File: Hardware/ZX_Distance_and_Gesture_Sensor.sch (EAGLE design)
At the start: 48 parts, among them Q1 MMBT2222A, Q2 MOSFET-NCHANNEL2N7002PW, U1 BRM-2508VERT

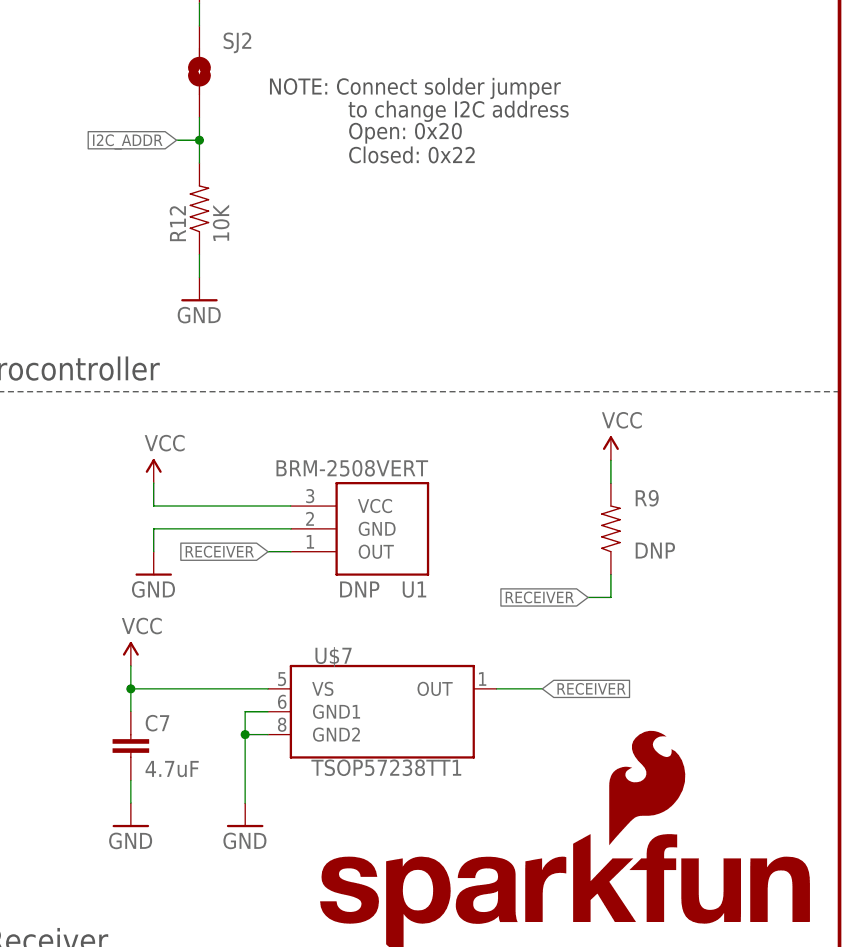
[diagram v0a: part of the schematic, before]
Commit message: Changed SMT receiver to DNP and removed DNP from PTH receiver and pullup resistor.
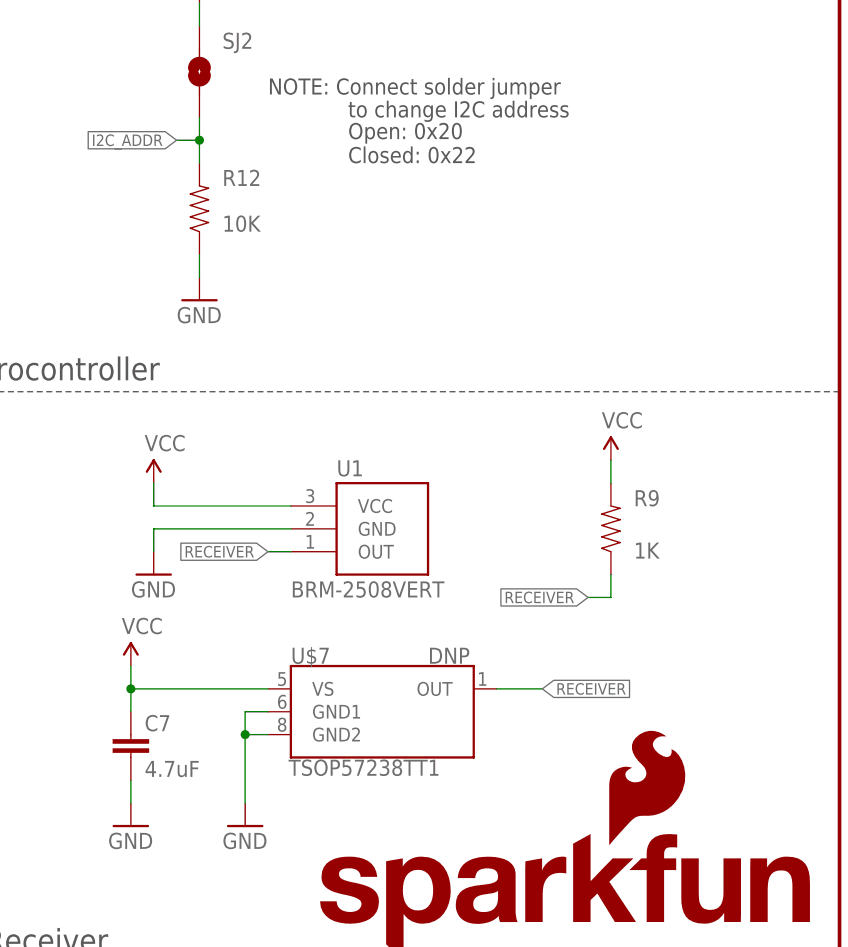
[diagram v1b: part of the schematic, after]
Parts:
- R9: value DNP -> 1K; device SparkFun-Resistors:RESISTOR0603 -> SparkFun-Resistors:1KOHM1/10W1%(0603)
- U$7: PLACE (none) -> DNP
- U1: PLACE DNP -> (none)
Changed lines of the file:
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@@
 <setting verticaltext="up"/>
 </settings>
-<grid distance="0.1" unitdist="inch" unit="inch" style="lines" multiple="1" display="no" altdistance="0.01" altunitdist="inch" altunit="inch"/>
+<grid distance="0.1" unitdist="inch" unit="inch" style="lines" multiple="1" display="yes" altdistance="0.01" altunitdist="inch" altunit="inch"/>
 <layers>
 <layer number="1" name="Top" color="4" fill="1" visible="no" active="no"/>
@@
 <part name="U$3" library="SparkFun-DiscreteSemi" deviceset="DMC2700UDM" device=""/>
 <part name="U$4" library="SparkFun-DiscreteSemi" deviceset="DMC2700UDM" device=""/>
-<part name="U$7" library="SparkFun-Sensors" deviceset="TSOP57238TT1" device=""/>
+<part name="U$7" library="SparkFun-Sensors" deviceset="TSOP57238TT1" device="">
+<attribute name="PLACE" value="DNP"/>
+</part>
 <part name="JP1" library="SparkFun-Connectors" deviceset="M06" device="NO_SILK"/>
 <part name="JP3" library="SparkFun-Connectors" deviceset="M03" device="1X03_NO_SILK"/>
@@
 <part name="SUPPLY10" library="SparkFun-Aesthetics" deviceset="VCC" device=""/>
 <part name="GND10" library="SparkFun-Aesthetics" deviceset="GND" device=""/>
-<part name="R9" library="SparkFun-Resistors" deviceset="RESISTOR" device="0603" value="DNP"/>
+<part name="R9" library="SparkFun-Resistors" deviceset="1KOHM1/10W1%(0603)" device="" value="1K"/>
 <part name="C7" library="SparkFun-Capacitors" deviceset="4.7UF-6.3V-10%(0603)" device="0603" value="4.7uF"/>
 <part name="GND11" library="SparkFun-Aesthetics" deviceset="GND" device=""/>
@@
 <part name="TP4" library="SparkFun-Passives" deviceset="TEST-POINT" device="3X4" value="TEST-POINT3X4"/>
 <part name="TP5" library="SparkFun-Passives" deviceset="TEST-POINT" device="3X4" value="TEST-POINT3X4"/>
-<part name="U1" library="SparkFun-Sensors" deviceset="BRM-2508" device="VERT">
-<attribute name="PLACE" value="DNP"/>
-</part>
+<part name="U1" library="SparkFun-Sensors" deviceset="BRM-2508" device="VERT"/>
 <part name="SUPPLY16" library="SparkFun-Aesthetics" deviceset="VCC" device=""/>
 <part name="GND16" library="SparkFun-Aesthetics" deviceset="GND" device=""/>
@@
 <instance part="U$3" gate="G$1" x="22.86" y="111.76"/>
 <instance part="U$4" gate="G$1" x="88.9" y="111.76"/>
-<instance part="U$7" gate="G$1" x="198.12" y="63.5"/>
+<instance part="U$7" gate="G$1" x="198.12" y="63.5" smashed="yes">
+<attribute name="NAME" x="187.96" y="68.834" size="1.778" layer="95"/>
+<attribute name="VALUE" x="187.706" y="56.388" size="1.778" layer="96"/>
+<attribute name="PLACE" x="203.2" y="68.834" size="1.778" layer="96"/>
+</instance>
 <instance part="JP1" gate="G$1" x="12.7" y="154.94" smashed="yes">
 <attribute name="VALUE" x="7.62" y="144.78" size="1.778" layer="96"/>
@@
 </instance>
 <instance part="SUPPLY13" gate="G$1" x="73.66" y="177.8"/>
-<instance part="R12" gate="G$1" x="177.8" y="119.38" rot="R90"/>
+<instance part="R12" gate="G$1" x="177.8" y="119.38" smashed="yes" rot="R90">
+<attribute name="NAME" x="180.34" y="121.92" size="1.778" layer="95"/>
+<attribute name="VALUE" x="180.34" y="116.84" size="1.778" layer="96"/>
+</instance>
 <instance part="GND15" gate="1" x="177.8" y="109.22"/>
 <instance part="SJ2" gate="1" x="177.8" y="134.62" smashed="yes" rot="R90">
@@
 </instance>
 <instance part="U1" gate="G$1" x="198.12" y="83.82" smashed="yes" rot="R180">
-<attribute name="PLACE" x="197.866" y="77.978" size="1.778" layer="96" rot="R180"/>
-<attribute name="NAME" x="203.2" y="77.978" size="1.778" layer="95" rot="R180"/>
-<attribute name="VALUE" x="203.2" y="91.44" size="1.778" layer="96" rot="R180"/>
+<attribute name="NAME" x="193.04" y="89.662" size="1.778" layer="95"/>
+<attribute name="VALUE" x="187.96" y="76.2" size="1.778" layer="96"/>
 </instance>
 <instance part="SUPPLY16" gate="G$1" x="172.72" y="88.9"/>

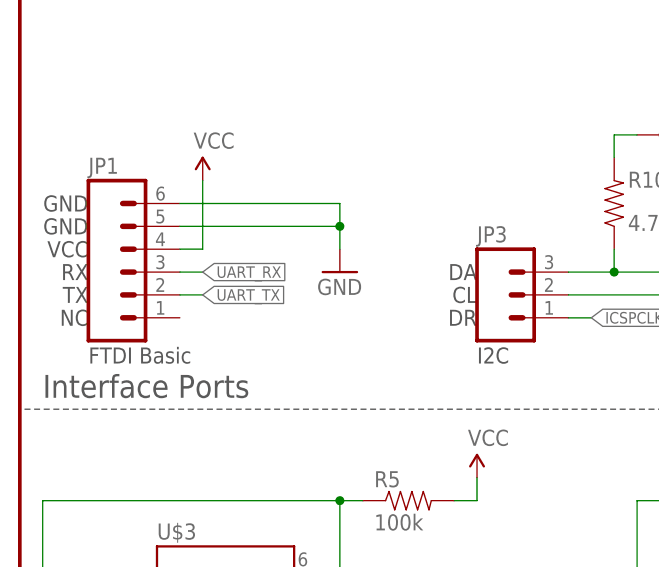
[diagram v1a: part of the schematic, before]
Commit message: Swapped TX/RX. Added diagonal trace from GND header to pour.
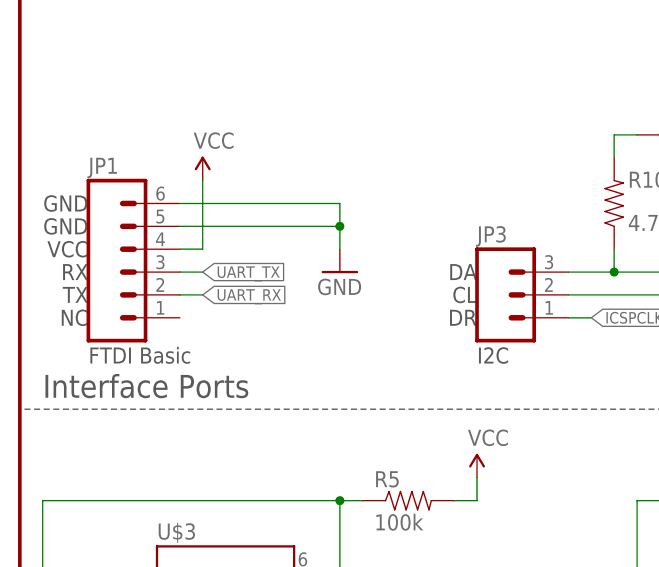
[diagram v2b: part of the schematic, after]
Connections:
- net UART_RX: now also JP1.2; no longer JP1.3
- net UART_TX: now also JP1.3; no longer JP1.2
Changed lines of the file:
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@@
 <net name="UART_TX" class="0">
+<segment>
+<pinref part="U$1" gate="G$1" pin="RC5"/>
+<wire x1="220.98" y1="157.48" x2="223.52" y2="157.48" width="0.1524" layer="91"/>
+<label x="223.52" y="157.48" size="1.27" layer="95" xref="yes"/>
+</segment>
+<segment>
+<pinref part="JP1" gate="G$1" pin="3"/>
+<wire x1="17.78" y1="154.94" x2="20.32" y2="154.94" width="0.1524" layer="91"/>
+<label x="20.32" y="154.94" size="1.27" layer="95" xref="yes"/>
+</segment>
+</net>
+<net name="UART_RX" class="0">
+<segment>
+<pinref part="U$1" gate="G$1" pin="RC4"/>
+<wire x1="220.98" y1="160.02" x2="223.52" y2="160.02" width="0.1524" layer="91"/>
+<label x="223.52" y="160.02" size="1.27" layer="95" xref="yes"/>
+</segment>
 <segment>
 <pinref part="JP1" gate="G$1" pin="2"/>
@@
 <label x="20.32" y="152.4" size="1.27" layer="95" xref="yes"/>
 </segment>
-<segment>
-<pinref part="U$1" gate="G$1" pin="RC5"/>
-<wire x1="220.98" y1="157.48" x2="223.52" y2="157.48" width="0.1524" layer="91"/>
-<label x="223.52" y="157.48" size="1.27" layer="95" xref="yes"/>
-</segment>
 </net>
-<net name="UART_RX" class="0">
-<segment>
-<pinref part="JP1" gate="G$1" pin="3"/>
-<wire x1="17.78" y1="154.94" x2="20.32" y2="154.94" width="0.1524" layer="91"/>
-<label x="20.32" y="154.94" size="1.27" layer="95" xref="yes"/>
-</segment>
-<segment>
-<pinref part="U$1" gate="G$1" pin="RC4"/>
-<wire x1="220.98" y1="160.02" x2="223.52" y2="160.02" width="0.1524" layer="91"/>
-<label x="223.52" y="160.02" size="1.27" layer="95" xref="yes"/>
-</segment>
-</net>

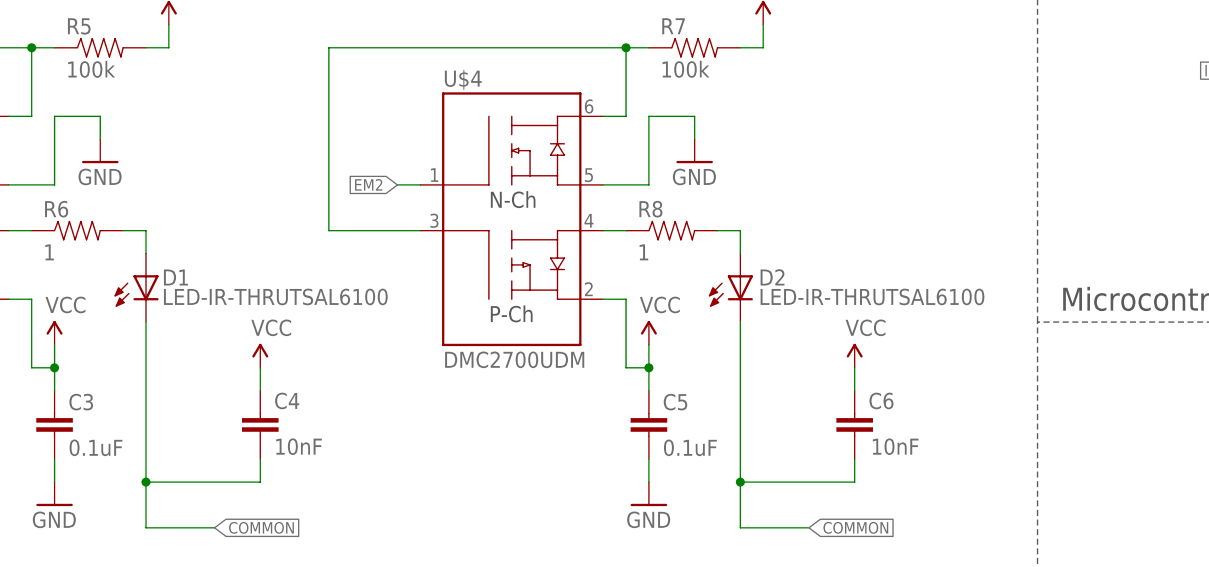
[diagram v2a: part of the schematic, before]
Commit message: Removed variant names on IR LEDs in schematic
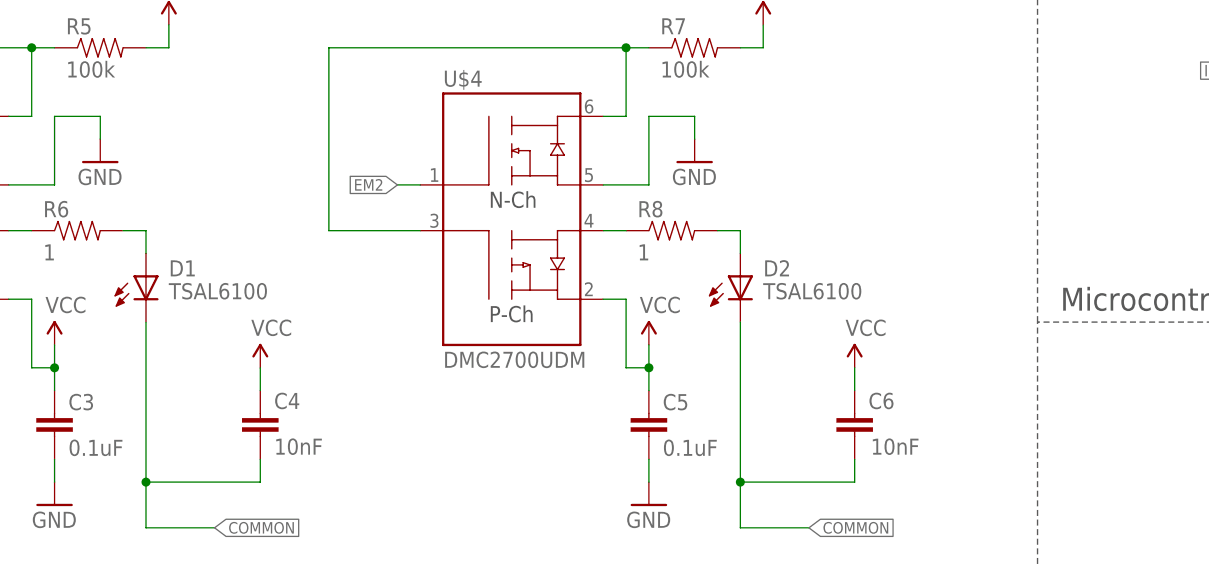
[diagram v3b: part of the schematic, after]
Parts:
- D1, D2: VARIANT (none) -> TSAL6100
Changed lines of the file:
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@@
 <part name="GND5" library="SparkFun-Aesthetics" deviceset="GND" device=""/>
 <part name="GND6" library="SparkFun-Aesthetics" deviceset="GND" device=""/>
-<part name="D1" library="SparkFun-LED" deviceset="LED-IR-THRU" device="TSAL6100" value="LED-IR-THRUTSAL6100"/>
+<part name="D1" library="SparkFun-LED" deviceset="LED-IR-THRU" device="TSAL6100" value="LED-IR-THRUTSAL6100">
+<attribute name="VARIANT" value="TSAL6100"/>
+</part>
 <part name="R5" library="SparkFun-Resistors" deviceset="100KOHM1/10W1%(0603)" device="" value="100k"/>
 <part name="R6" library="SparkFun-Resistors" deviceset="1OHM1/10W1%(0603)" device="" value="1"/>
@@
 <part name="GND11" library="SparkFun-Aesthetics" deviceset="GND" device=""/>
 <part name="SUPPLY11" library="SparkFun-Aesthetics" deviceset="VCC" device=""/>
-<part name="D2" library="SparkFun-LED" deviceset="LED-IR-THRU" device="TSAL6100" value="LED-IR-THRUTSAL6100"/>
+<part name="D2" library="SparkFun-LED" deviceset="LED-IR-THRU" device="TSAL6100" value="LED-IR-THRUTSAL6100">
+<attribute name="VARIANT" value="TSAL6100"/>
+</part>
 <part name="SUPPLY12" library="SparkFun-Aesthetics" deviceset="VCC" device=""/>
 <part name="GND12" library="SparkFun-Aesthetics" deviceset="GND" device=""/>
@@
 <instance part="GND6" gate="1" x="91.44" y="5.08"/>
 <instance part="D1" gate="G$1" x="48.26" y="104.14" smashed="yes">
-<attribute name="NAME" x="50.038" y="103.124" size="1.778" layer="95"/>
-<attribute name="VALUE" x="50.038" y="100.965" size="1.778" layer="96"/>
+<attribute name="NAME" x="50.8" y="104.14" size="1.778" layer="95"/>
+<attribute name="VARIANT" x="50.8" y="101.6" size="1.778" layer="96"/>
 </instance>
 <instance part="R5" gate="G$1" x="43.18" y="129.54"/>
@@
 <instance part="SUPPLY11" gate="G$1" x="170.18" y="68.58"/>
 <instance part="D2" gate="G$1" x="114.3" y="104.14" smashed="yes">
-<attribute name="NAME" x="116.332" y="103.124" size="1.778" layer="95"/>
-<attribute name="VALUE" x="116.332" y="100.965" size="1.778" layer="96"/>
+<attribute name="NAME" x="116.84" y="104.14" size="1.778" layer="95"/>
+<attribute name="VARIANT" x="116.84" y="101.6" size="1.778" layer="96"/>
 </instance>
 <instance part="SUPPLY12" gate="G$1" x="223.52" y="91.44"/>
